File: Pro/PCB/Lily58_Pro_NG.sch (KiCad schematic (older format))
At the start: 87 parts, among them J1 LED, J2 4PIN, J3 OLED, P1 i2c_pin, P2 i2c_pin, SW1 SW_PUSH, SW10 SW_PUSH, SW11 SW_PUSH, SW12 SW_PUSH, SW13 SW_PUSH, SW14 SW_PUSH, SW15 SW_PUSH, SW16 SW_PUSH, SW17 SW_PUSH, SW18 SW_PUSH, SW19 SW_PUSH, SW2 SW_PUSH, SW20 SW_PUSH, SW21 SW_PUSH, SW22 SW_PUSH, SW23 SW_PUSH, SW24 SW_PUSH, SW25 SW_PUSH, SW26 SW_PUSH, SW27 SW_PUSH, SW28 SW_PUSH, SW29 SW_PUSH, SW3 SW_PUSH, SW30 SW_PUSH, SW31 Rotary_Encoder_Switch, SW4 SW_PUSH, SW5 SW_PUSH, SW6 SW_PUSH, SW7 SW_PUSH, SW8 SW_PUSH, SW9 SW_PUSH, U1 ProMicro

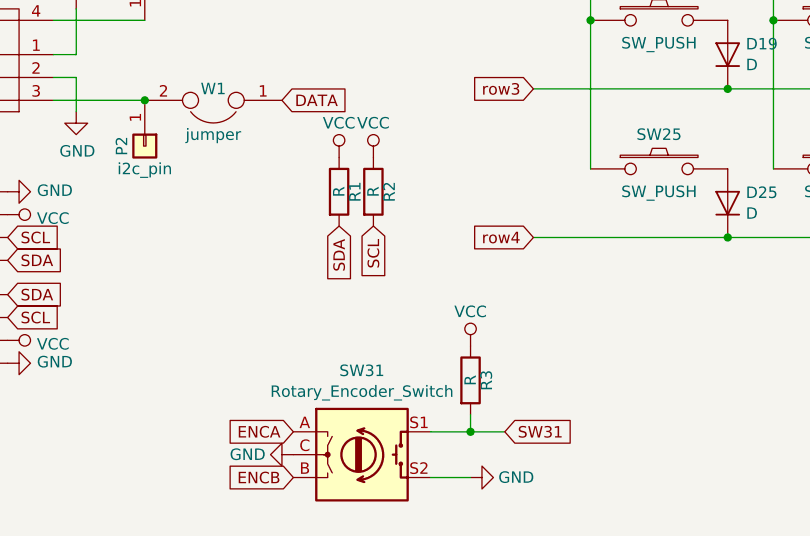
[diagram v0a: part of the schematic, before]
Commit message: Final version of Lily60 Evo PCB and Case
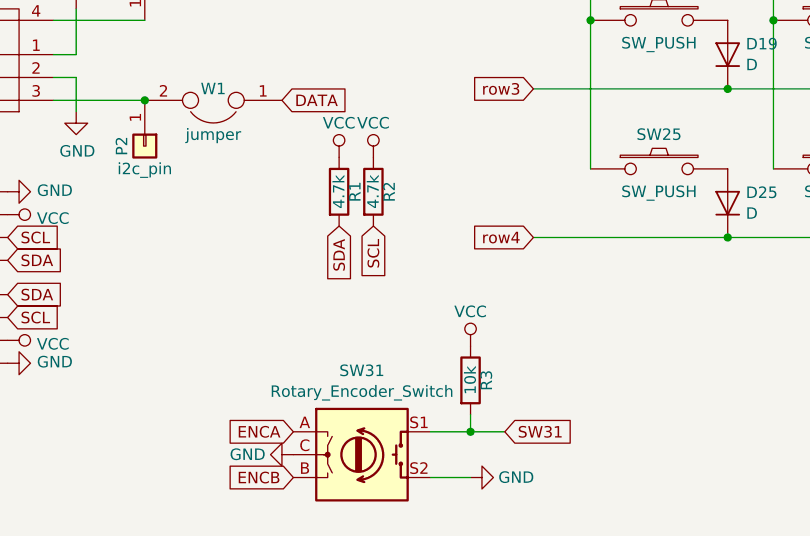
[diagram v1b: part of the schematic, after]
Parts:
- R1, R2: value R -> 4.7k
- R3: value R -> 10k
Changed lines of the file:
@@
 P 4400 4950
 F 0 "R1" V 4500 4950 50  0000 C BNN
-F 1 "R" V 4400 4950 50  0000 C CNN
+F 1 "4.7k" V 4400 4950 50  0000 C CNN
 F 2 "Lily58_Pro-footprint:RESISTOR_mini" V 4330 4950 50  0001 C CNN
 F 3 "" H 4400 4950 50  0001 C CNN
@@
 P 4550 4950
 F 0 "R2" V 4650 4950 50  0000 C BNN
-F 1 "R" V 4550 4950 50  0000 C CNN
+F 1 "4.7k" V 4550 4950 50  0000 C CNN
 F 2 "Lily58_Pro-footprint:RESISTOR_mini" V 4480 4950 50  0001 C CNN
 F 3 "" H 4550 4950 50  0001 C CNN
@@
 P 4975 5775
 F 0 "R3" V 5075 5775 50  0000 C BNN
-F 1 "R" V 4975 5775 50  0000 C CNN
+F 1 "10k" V 4975 5775 50  0000 C CNN
 F 2 "Lily58_Pro-footprint:RESISTOR_mini" V 4905 5775 50  0001 C CNN
 F 3 "" H 4975 5775 50  0001 C CNN

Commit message: SW31 can be an encoder or a MW Switch
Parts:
- removed R3: 10k, Lily58_Pro-footprint:RESISTOR_mini, symbol Lily58_Pro-rescue:R-Lily58-cache
- added D31: D, Lily58_Pro-footprint:Diode_SOD123, symbol Lily58_Pro-rescue:D-Lily58-cache
- SW31: footprint Keebio-parts:RotaryEncoder_EC11 -> Lily58_Pro-footprint:SW_MX_Reveresible_RotaryEncoder_EC11; symbol Device:Rotary_Encoder_Switch -> Lily58_Pro-rescue:Rotary_Encoder_Switch
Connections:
- net GND: no longer SW31.S2
- net col0: now also SW31.1
- net SW31 renamed row5
- net row5: now also D31.1 (K); no longer SW31.S1
- new net: D31.2 (A), SW31.2
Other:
- moved on the sheet: SW31, TH1, TH2, TH3, TH4, TH5, TH6, TH7
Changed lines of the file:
@@
 L Lily58_Pro-rescue:HOLE-Lily58-cache TH1
 U 1 1 5B74CE27
-P 7100 6150
-F 0 "TH1" H 7100 6150 60  0000 C CNN
-F 1 "HOLE" H 7100 6050 60  0000 C CNN
-F 2 "Lily58-footprint:M2_HOLE_PCB" H 7100 6150 60  0001 C CNN
-F 3 "" H 7100 6150 60  0000 C CNN
-	1    7100 6150
+P 3525 7350
+F 0 "TH1" H 3525 7350 60  0000 C CNN
+F 1 "HOLE" H 3525 7250 60  0000 C CNN
+F 2 "Lily58-footprint:M2_HOLE_PCB" H 3525 7350 60  0001 C CNN
+F 3 "" H 3525 7350 60  0000 C CNN
+	1    3525 7350
 	1    0    0    -1
 $EndComp
@@
 L Lily58_Pro-rescue:HOLE-Lily58-cache TH2
 U 1 1 5B74D0C7
-P 7450 6150
-F 0 "TH2" H 7450 6150 60  0000 C CNN
-F 1 "HOLE" H 7450 6050 60  0000 C CNN
-F 2 "Lily58-footprint:M2_HOLE_PCB" H 7450 6150 60  0001 C CNN
-F 3 "" H 7450 6150 60  0000 C CNN
-	1    7450 6150
+P 3875 7350
+F 0 "TH2" H 3875 7350 60  0000 C CNN
+F 1 "HOLE" H 3875 7250 60  0000 C CNN
+F 2 "Lily58-footprint:M2_HOLE_PCB" H 3875 7350 60  0001 C CNN
+F 3 "" H 3875 7350 60  0000 C CNN
+	1    3875 7350
 	1    0    0    -1
 $EndComp
@@
 L Lily58_Pro-rescue:HOLE-Lily58-cache TH4
 U 1 1 5B74D1C0
-P 8450 6150
-F 0 "TH4" H 8450 6150 60  0000 C CNN
-F 1 "HOLE" H 8450 6050 60  0000 C CNN
-F 2 "Lily58_Pro-footprint:HOLE_M2_TH" H 8450 6150 60  0001 C CNN
-F 3 "" H 8450 6150 60  0000 C CNN
-	1    8450 6150
+P 4875 7350
+F 0 "TH4" H 4875 7350 60  0000 C CNN
+F 1 "HOLE" H 4875 7250 60  0000 C CNN
+F 2 "Lily58_Pro-footprint:HOLE_M2_TH" H 4875 7350 60  0001 C CNN
+F 3 "" H 4875 7350 60  0000 C CNN
+	1    4875 7350
 	1    0    0    -1
 $EndComp
@@
 L Lily58_Pro-rescue:HOLE-Lily58-cache TH5
 U 1 1 5B74D78B
-P 8800 6150
-F 0 "TH5" H 8800 6150 60  0000 C CNN
-F 1 "HOLE" H 8800 6050 60  0000 C CNN
-F 2 "Lily58_Pro-footprint:HOLE_M2_TH" H 8800 6150 60  0001 C CNN
-F 3 "" H 8800 6150 60  0000 C CNN
-	1    8800 6150
+P 5225 7350
+F 0 "TH5" H 5225 7350 60  0000 C CNN
+F 1 "HOLE" H 5225 7250 60  0000 C CNN
+F 2 "Lily58_Pro-footprint:HOLE_M2_TH" H 5225 7350 60  0001 C CNN
+F 3 "" H 5225 7350 60  0000 C CNN
+	1    5225 7350
 	1    0    0    -1
 $EndComp
@@
 L Lily58_Pro-rescue:HOLE-Lily58-cache TH6
 U 1 1 5B74D88C
-P 9150 6150
-F 0 "TH6" H 9150 6150 60  0000 C CNN
-F 1 "HOLE" H 9150 6050 60  0000 C CNN
-F 2 "Lily58_Pro-footprint:HOLE_M2_TH" H 9150 6150 60  0001 C CNN
-F 3 "" H 9150 6150 60  0000 C CNN
-	1    9150 6150
+P 5575 7350
+F 0 "TH6" H 5575 7350 60  0000 C CNN
+F 1 "HOLE" H 5575 7250 60  0000 C CNN
+F 2 "Lily58_Pro-footprint:HOLE_M2_TH" H 5575 7350 60  0001 C CNN
+F 3 "" H 5575 7350 60  0000 C CNN
+	1    5575 7350
 	1    0    0    -1
 $EndComp
@@
 L Lily58_Pro-rescue:HOLE-Lily58-cache TH7
 U 1 1 5B74D98F
-P 9500 6150
-F 0 "TH7" H 9500 6150 60  0000 C CNN
-F 1 "HOLE" H 9500 6050 60  0000 C CNN
-F 2 "Lily58_Pro-footprint:HOLE_M2_TH" H 9500 6150 60  0001 C CNN
-F 3 "" H 9500 6150 60  0000 C CNN
-	1    9500 6150
+P 5925 7350
+F 0 "TH7" H 5925 7350 60  0000 C CNN
+F 1 "HOLE" H 5925 7250 60  0000 C CNN
+F 2 "Lily58_Pro-footprint:HOLE_M2_TH" H 5925 7350 60  0001 C CNN
+F 3 "" H 5925 7350 60  0000 C CNN
+	1    5925 7350
 	1    0    0    -1
 $EndComp
@@
 L Lily58_Pro-rescue:HOLE-Lily58-cache TH3
 U 1 1 5B74DA95
-P 8100 6150
-F 0 "TH3" H 8100 6150 60  0000 C CNN
-F 1 "HOLE" H 8100 6050 60  0000 C CNN
-F 2 "Lily58_Pro-footprint:HOLE_M2_TH" H 8100 6150 60  0001 C CNN
-F 3 "" H 8100 6150 60  0000 C CNN
-	1    8100 6150
+P 4525 7350
+F 0 "TH3" H 4525 7350 60  0000 C CNN
+F 1 "HOLE" H 4525 7250 60  0000 C CNN
+F 2 "Lily58_Pro-footprint:HOLE_M2_TH" H 4525 7350 60  0001 C CNN
+F 3 "" H 4525 7350 60  0000 C CNN
+	1    4525 7350
 	1    0    0    -1
 $EndComp
@@
 L Lily58_Pro-rescue:PWR_FLAG-Lily58-cache #FLG02
 U 1 1 5B74C9D1
-P 10250 6150
-F 0 "#FLG02" H 10250 6225 50  0001 C CNN
-F 1 "PWR_FLAG" H 10250 6323 50  0000 C CNN
-F 2 "" H 10250 6150 50  0001 C CNN
-F 3 "" H 10250 6150 50  0001 C CNN
-	1    10250 6150
+P 6675 7350
+F 0 "#FLG02" H 6675 7425 50  0001 C CNN
+F 1 "PWR_FLAG" H 6675 7523 50  0000 C CNN
+F 2 "" H 6675 7350 50  0001 C CNN
+F 3 "" H 6675 7350 50  0001 C CNN
+	1    6675 7350
 	-1   0    0    1
 $EndComp
@@
 L Lily58_Pro-rescue:VCC-Lily58-cache #PWR013
 U 1 1 5B74C8DE
-P 10250 6150
-F 0 "#PWR013" H 10250 6000 50  0001 C CNN
-F 1 "VCC" H 10267 6323 50  0000 C CNN
-F 2 "" H 10250 6150 50  0001 C CNN
-F 3 "" H 10250 6150 50  0001 C CNN
-	1    10250 6150
+P 6675 7350
+F 0 "#PWR013" H 6675 7200 50  0001 C CNN
+F 1 "VCC" H 6692 7523 50  0000 C CNN
+F 2 "" H 6675 7350 50  0001 C CNN
+F 3 "" H 6675 7350 50  0001 C CNN
+	1    6675 7350
 	1    0    0    -1
 $EndComp
@@
 L Lily58_Pro-rescue:GND-Lily58-cache #PWR012
 U 1 1 5B74C7EB
-P 9900 6150
-F 0 "#PWR012" H 9900 5900 50  0001 C CNN
-F 1 "GND" H 9905 5977 50  0000 C CNN
-F 2 "" H 9900 6150 50  0001 C CNN
-F 3 "" H 9900 6150 50  0001 C CNN
-	1    9900 6150
+P 6325 7350
+F 0 "#PWR012" H 6325 7100 50  0001 C CNN
+F 1 "GND" H 6330 7177 50  0000 C CNN
+F 2 "" H 6325 7350 50  0001 C CNN
+F 3 "" H 6325 7350 50  0001 C CNN
+	1    6325 7350
 	1    0    0    -1
 $EndComp
@@
 L Lily58_Pro-rescue:PWR_FLAG-Lily58-cache #FLG01
 U 1 1 5B74C681
-P 9900 6150
-F 0 "#FLG01" H 9900 6225 50  0001 C CNN
-F 1 "PWR_FLAG" H 9900 6324 50  0000 C CNN
-F 2 "" H 9900 6150 50  0001 C CNN
-F 3 "" H 9900 6150 50  0001 C CNN
-	1    9900 6150
-	1    0    0    -1
-$EndComp
-$Comp
-L Device:Rotary_Encoder_Switch SW31
+P 6325 7350
+F 0 "#FLG01" H 6325 7425 50  0001 C CNN
+F 1 "PWR_FLAG" H 6325 7524 50  0000 C CNN
+F 2 "" H 6325 7350 50  0001 C CNN
+F 3 "" H 6325 7350 50  0001 C CNN
+	1    6325 7350
+	1    0    0    -1
+$EndComp
+$Comp
+L Lily58_Pro-rescue:Rotary_Encoder_Switch SW31
 U 1 1 5EC9DC0C
-P 4500 6100
-F 0 "SW31" H 4500 6467 50  0000 C CNN
-F 1 "Rotary_Encoder_Switch" H 4500 6376 50  0000 C CNN
-F 2 "Keebio-parts:RotaryEncoder_EC11" H 4350 6260 50  0001 C CNN
-F 3 "~" H 4500 6360 50  0001 C CNN
-	1    4500 6100
-	1    0    0    -1
-$EndComp
-$Comp
-L Lily58_Pro-rescue:VCC-Lily58-cache #PWR0103
-U 1 1 5EC9FA66
-P 4975 5625
-F 0 "#PWR0103" H 4975 5475 50  0001 C CNN
-F 1 "VCC" H 4975 5775 50  0000 C CNN
-F 2 "" H 4975 5625 50  0001 C CNN
-F 3 "" H 4975 5625 50  0001 C CNN
-	1    4975 5625
-	1    0    0    -1
-$EndComp
-$Comp
-L Lily58_Pro-rescue:R-Lily58-cache R3
-U 1 1 5EC9FA70
-P 4975 5775
-F 0 "R3" V 5075 5775 50  0000 C BNN
-F 1 "10k" V 4975 5775 50  0000 C CNN
-F 2 "Lily58_Pro-footprint:RESISTOR_mini" V 4905 5775 50  0001 C CNN
-F 3 "" H 4975 5775 50  0001 C CNN
-	1    4975 5775
-	1    0    0    -1
-$EndComp
-Text GLabel 5125 6000 2    50   Input ~ 0
-SW31
-Wire Wire Line
-	4800 6000 4975 6000
-Wire Wire Line
-	4975 5925 4975 6000
-Connection ~ 4975 6000
-Wire Wire Line
-	4975 6000 5125 6000
-Wire Wire Line
-	4800 6200 4975 6200
-$Comp
-L Lily58_Pro-rescue:GND-Lily58-cache #PWR0104
-U 1 1 5ECAE063
-P 4975 6200
-F 0 "#PWR0104" H 4975 5950 50  0001 C CNN
-F 1 "GND" V 4975 6000 50  0000 C CNN
-F 2 "" H 4975 6200 50  0001 C CNN
-F 3 "" H 4975 6200 50  0001 C CNN
-	1    4975 6200
-	0    -1   -1   0
-$EndComp
+P 9900 5550
+F 0 "SW31" H 9900 5800 50  0000 C CNN
+F 1 "Rotary_Encoder_Switch" H 9700 5275 50  0000 C CNN
+F 2 "Lily58_Pro-footprint:SW_MX_Reveresible_RotaryEncoder_EC11" H 9750 5710 50  0001 C CNN
+F 3 "~" H 9900 5810 50  0001 C CNN
+	1    9900 5550
+	-1   0    0    -1
+$EndComp
+Text GLabel 9025 5875 0    50   Input ~ 0
+row5
 Text GLabel 2550 2700 0    50   Input ~ 0
-SW31
-Text GLabel 4200 6000 0    50   Input ~ 0
+row5
+Text GLabel 10200 5450 2    50   Input ~ 0
 ENCA
-Text GLabel 4200 6200 0    50   Input ~ 0
+Text GLabel 10200 5650 2    50   Input ~ 0
 ENCB
 Text GLabel 3850 2500 2    50   Input ~ 0
@@
 L Lily58_Pro-rescue:GND-Lily58-cache #PWR0105
 U 1 1 5ECB806A
-P 4200 6100
-F 0 "#PWR0105" H 4200 5850 50  0001 C CNN
-F 1 "GND" V 4200 5900 50  0000 C CNN
-F 2 "" H 4200 6100 50  0001 C CNN
-F 3 "" H 4200 6100 50  0001 C CNN
-	1    4200 6100
-	0    1    1    0
-$EndComp
+P 10200 5550
+F 0 "#PWR0105" H 10200 5300 50  0001 C CNN
+F 1 "GND" V 10200 5350 50  0000 C CNN
+F 2 "" H 10200 5550 50  0001 C CNN
+F 3 "" H 10200 5550 50  0001 C CNN
+	1    10200 5550
+	0    -1   1    0
+$EndComp
+$Comp
+L Lily58_Pro-rescue:D-Lily58-cache D31
+U 1 1 5EC2CFC4
+P 9350 5875
+F 0 "D31" V 9396 5796 50  0000 R CNN
+F 1 "D" V 9305 5796 50  0000 R CNN
+F 2 "Lily58_Pro-footprint:Diode_SOD123" H 9350 5875 50  0001 C CNN
+F 3 "" H 9350 5875 50  0001 C CNN
+	1    9350 5875
+	1    0    0    1
+$EndComp
+Wire Wire Line
+	9500 4850 9500 5450
+Connection ~ 9500 4850
+Wire Wire Line
+	9025 5875 9200 5875
+Wire Wire Line
+	9500 5450 9600 5450
+Wire Wire Line
+	9600 5650 9600 5875
+Wire Wire Line
+	9600 5875 9500 5875
 $EndSCHEMATC
